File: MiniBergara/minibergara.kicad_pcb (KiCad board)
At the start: 2 copper layers, 12 parts, among them SW1 SW_Nidec_CAS-120A1, U1 TB6612_BREAKOUT, U3 AMS1117-1.5

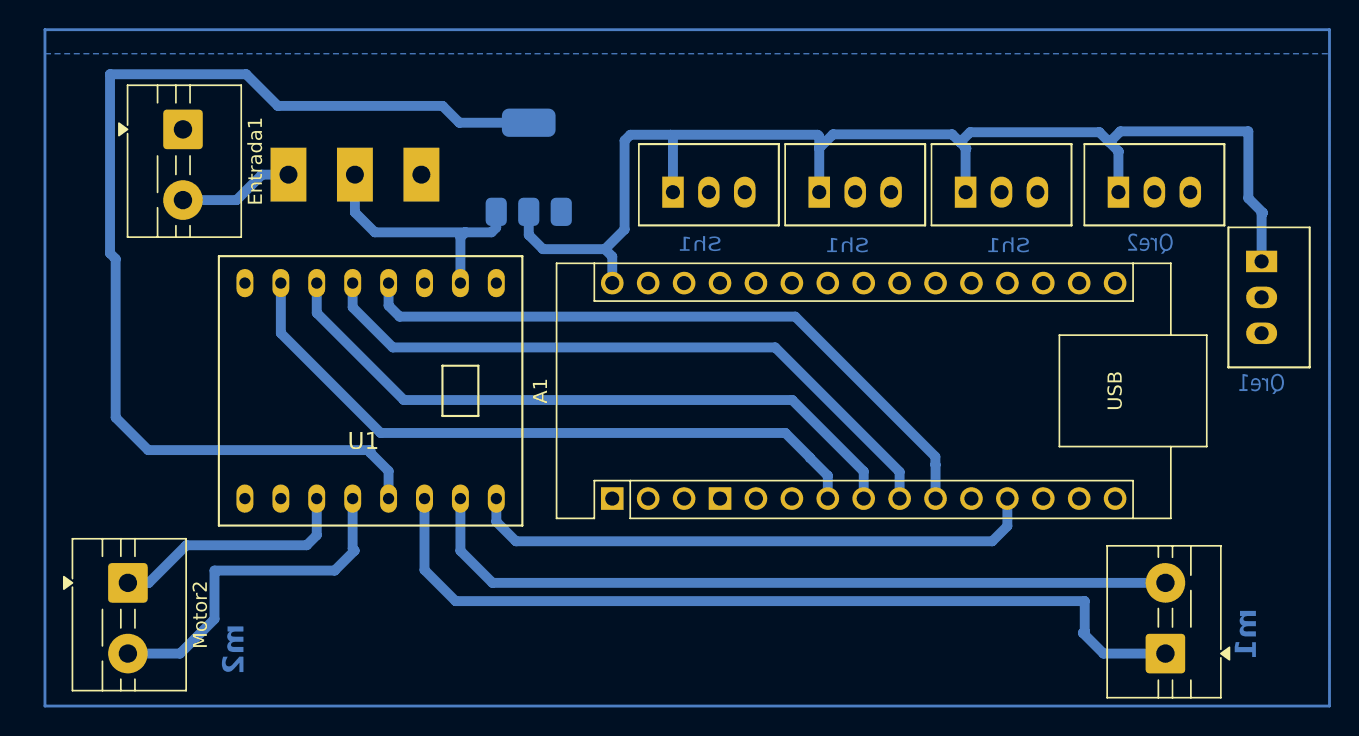
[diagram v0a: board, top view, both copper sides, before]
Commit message: falta mover nano
move el nano abajo con las pistas
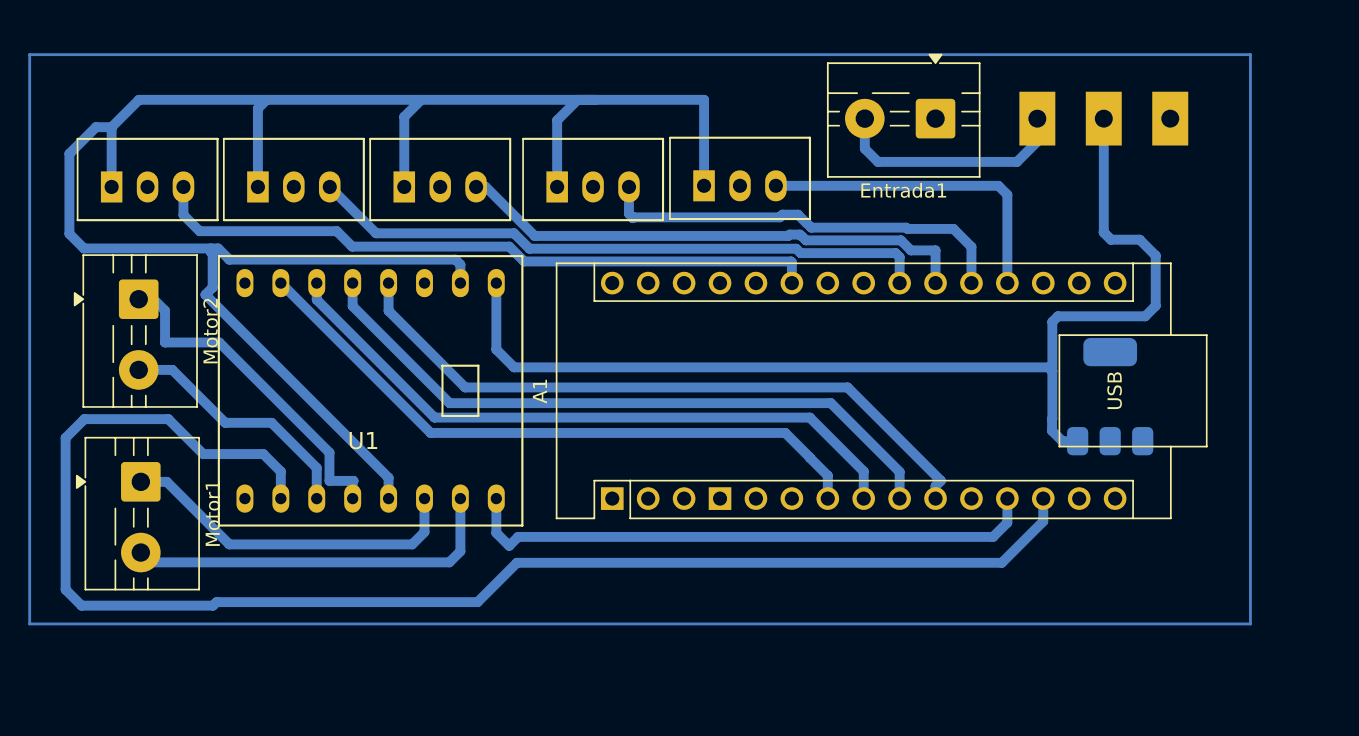
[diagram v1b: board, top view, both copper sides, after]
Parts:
- moved Motor1 73.5 mm to (80.8, 77.1), turned to -90 degrees
- moved Entrada1 53.2 mm to (137.0, 51.4), turned to 180 degrees
- moved SW1 53.1 mm to (148.9, 51.4)
- moved U3 44.2 mm to (149.3, 71.1)
- moved Sharp1 39.7 mm to (81.3, 56.2)
- moved Sharp2 39.7 mm to (91.6, 56.2)
- moved Sharp3 39.7 mm to (102.0, 56.2)
- moved sensorpiso2 39.7 mm to (112.8, 56.2)
- moved sensorpiso1 37.7 mm to (123.2, 56.1), turned to 0 degrees
- moved Motor2 20.1 mm to (80.7, 64.2)
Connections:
- A1 pad 13: unconnected-(A1-D10-Pad13) -> PWMB
- A1 pad 30: +5V -> VCC
- U1 pad 1: unconnected-(U1-VM-Pad1) -> VCC
- U1 pad 11: M2a -> M2b
- U1 pad 12: M2b -> M2a
- U1 pad 2: VCC -> +5V
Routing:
- net PWMB: track 0.00 -> 103.6 mm
- net VCC: track 18.2 -> 79.0 mm
- net Sh1: track 0.00 -> 47.9 mm
- net Sh2: track 0.00 -> 44.2 mm
- net M1a: track 61.4 -> 24.6 mm
- net Sh3: track 0.00 -> 36.7 mm
- net +5V: track 167.9 -> 136.7 mm
- net out2: track 0.00 -> 29.9 mm
- net M1b: track 54.5 -> 26.9 mm
- net out1: track 0.00 -> 22.9 mm
- net Net-(Entrada1-Pin_2): track 8.21 -> 16.9 mm
- net M2b: track 24.8 -> 17.6 mm
- net M2a: track 17.3 -> 24.3 mm
- net B2: track 48.0 -> 46.0 mm
- net PWMA: track 40.7 -> 41.3 mm
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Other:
- board text removed: "Qre1"
- board text removed: "Qre2"
- board text removed: "Sh1"
- board text removed: "m1"
- board text removed: "m2"
